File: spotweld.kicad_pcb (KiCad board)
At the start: 2 copper layers, 85.9 x 58.9 mm, 48 parts, among them J1 Conn_02x03_Odd_Even, J2 Conn_01x02, J5 Conn_01x02, Q1 IRF3205, Q2 IRF3205, Q3 IRF3205, Q4 IRF3205, Q5 IRF3205, Q6 IRF3205, Q7 IRF3205, Q8 IRF3205, SW1 SW_Push, U1 ATtiny24-20SSU, U2 TC4429VOA, U3 L78L05_SOT89

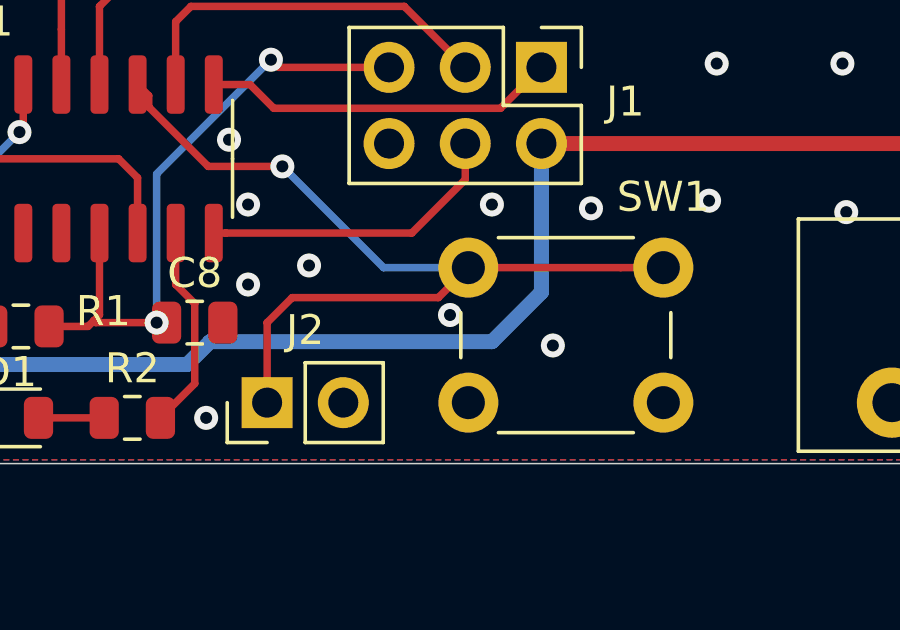
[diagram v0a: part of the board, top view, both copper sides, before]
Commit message: Correct via clearence
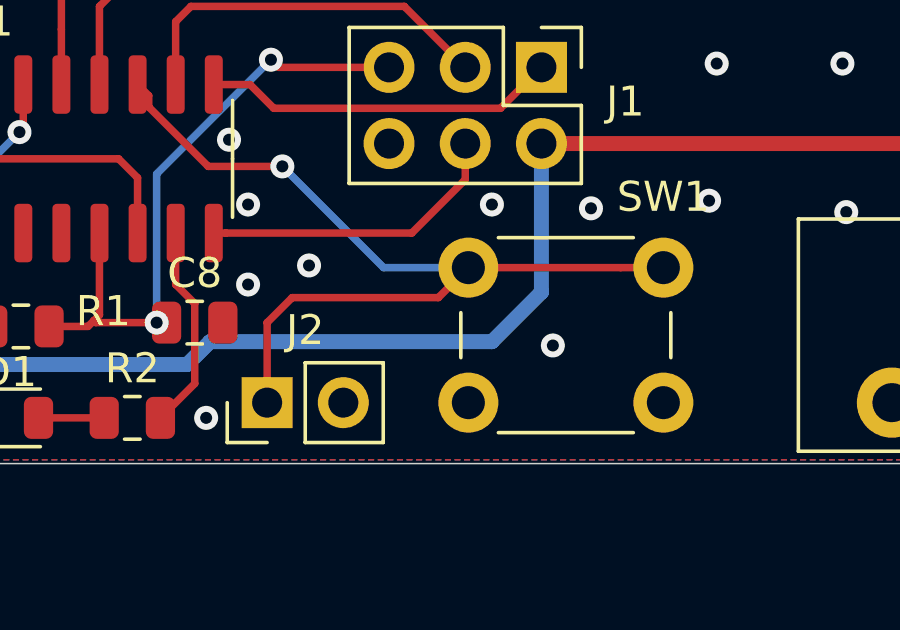
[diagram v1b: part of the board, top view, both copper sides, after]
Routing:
- net GND: vias 42 -> 41
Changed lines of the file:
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@@
     (thickness 1.6)
     (drawings 6)
-    (tracks 291)
+    (tracks 290)
     (zones 0)
     (modules 48)
@@
       (outputformat 1)
       (mirror false)
-      (drillshape 1)
+      (drillshape 0)
       (scaleselection 1)
-      (outputdirectory ""))
+      (outputdirectory "/mnt/store/Bango/ALLPROJECTS/spot-welder/spotweld/gerbers/"))
   )
   (net 0 "")
@@
     (add_net Vdrive)
   )
+  (module Button_Switch_THT:SW_PUSH_6mm_H5mm (layer F.Cu)
+    (at 151.892 119.634 180)
+    (descr "tactile push button, 6x6mm e.g. PHAP33xx series, height=5mm")
+    (tags "tact sw push 6mm")
+    (fp_text reference SW1 (at 0 6.858) (layer F.SilkS)
+      (effects (font (size 1 1) (thickness 0.15)))
+    )
+    (fp_text value SW_Push (at 3.75 6.7) (layer F.Fab)
+      (effects (font (size 1 1) (thickness 0.15)))
+    )
+    (fp_circle (center 3.25 2.25) (end 1.25 2.5) (layer F.Fab) (width 0.1))
+    (fp_line (start 6.75 3) (end 6.75 1.5) (layer F.SilkS) (width 0.12))
+    (fp_line (start 5.5 -1) (end 1 -1) (layer F.SilkS) (width 0.12))
+    (fp_line (start -0.25 1.5) (end -0.25 3) (layer F.SilkS) (width 0.12))
+    (fp_line (start 1 5.5) (end 5.5 5.5) (layer F.SilkS) (width 0.12))
+    (fp_line (start 8 -1.25) (end 8 5.75) (layer F.CrtYd) (width 0.05))
+    (fp_line (start 7.75 6) (end -1.25 6) (layer F.CrtYd) (width 0.05))
+    (fp_line (start -1.5 5.75) (end -1.5 -1.25) (layer F.CrtYd) (width 0.05))
+    (fp_line (start -1.25 -1.5) (end 7.75 -1.5) (layer F.CrtYd) (width 0.05))
+    (fp_line (start -1.5 6) (end -1.25 6) (layer F.CrtYd) (width 0.05))
+    (fp_line (start -1.5 5.75) (end -1.5 6) (layer F.CrtYd) (width 0.05))
+    (fp_line (start -1.5 -1.5) (end -1.25 -1.5) (layer F.CrtYd) (width 0.05))
+    (fp_line (start -1.5 -1.25) (end -1.5 -1.5) (layer F.CrtYd) (width 0.05))
+    (fp_line (start 8 -1.5) (end 8 -1.25) (layer F.CrtYd) (width 0.05))
+    (fp_line (start 7.75 -1.5) (end 8 -1.5) (layer F.CrtYd) (width 0.05))
+    (fp_line (start 8 6) (end 8 5.75) (layer F.CrtYd) (width 0.05))
+    (fp_line (start 7.75 6) (end 8 6) (layer F.CrtYd) (width 0.05))
+    (fp_line (start 0.25 -0.75) (end 3.25 -0.75) (layer F.Fab) (width 0.1))
+    (fp_line (start 0.25 5.25) (end 0.25 -0.75) (layer F.Fab) (width 0.1))
+    (fp_line (start 6.25 5.25) (end 0.25 5.25) (layer F.Fab) (width 0.1))
+    (fp_line (start 6.25 -0.75) (end 6.25 5.25) (layer F.Fab) (width 0.1))
+    (fp_line (start 3.25 -0.75) (end 6.25 -0.75) (layer F.Fab) (width 0.1))
+    (fp_text user %R (at 3.048 2.25) (layer F.Fab)
+      (effects (font (size 1 1) (thickness 0.15)))
+    )
+    (pad 1 thru_hole circle (at 6.5 0 270) (size 2 2) (drill 1.1) (layers *.Cu *.Mask)
+      (net 1 GND))
+    (pad 2 thru_hole circle (at 6.5 4.5 270) (size 2 2) (drill 1.1) (layers *.Cu *.Mask)
+      (net 17 "Net-(J2-Pad1)"))
+    (pad 1 thru_hole circle (at 0 0 270) (size 2 2) (drill 1.1) (layers *.Cu *.Mask)
+      (net 1 GND))
+    (pad 2 thru_hole circle (at 0 4.5 270) (size 2 2) (drill 1.1) (layers *.Cu *.Mask)
+      (net 17 "Net-(J2-Pad1)"))
+    (model ${KISYS3DMOD}/Button_Switch_THT.3dshapes/SW_PUSH_6mm_H5mm.wrl
+      (at (xyz 0 0 0))
+      (scale (xyz 1 1 1))
+      (rotate (xyz 0 0 0))
+    )
+  )
   (module Package_TO_SOT_THT:TO-220-3_Horizontal_TabDown (layer F.Cu)
     (at 181.864 82.804)
@@
       (net 2 VCC))
     (model ${KISYS3DMOD}/Package_SO.3dshapes/SOIC-14_3.9x8.7mm_P1.27mm.wrl
-      (at (xyz 0 0 0))
-      (scale (xyz 1 1 1))
-      (rotate (xyz 0 0 0))
-    )
-  )
-  (module Button_Switch_THT:SW_PUSH_6mm_H5mm (layer F.Cu)
-    (at 151.892 119.634 180)
-    (descr "tactile push button, 6x6mm e.g. PHAP33xx series, height=5mm")
-    (tags "tact sw push 6mm")
-    (fp_text reference SW1 (at 0 6.858) (layer F.SilkS)
-      (effects (font (size 1 1) (thickness 0.15)))
-    )
-    (fp_text value SW_Push (at 3.75 6.7) (layer F.Fab)
-      (effects (font (size 1 1) (thickness 0.15)))
-    )
-    (fp_circle (center 3.25 2.25) (end 1.25 2.5) (layer F.Fab) (width 0.1))
-    (fp_line (start 6.75 3) (end 6.75 1.5) (layer F.SilkS) (width 0.12))
-    (fp_line (start 5.5 -1) (end 1 -1) (layer F.SilkS) (width 0.12))
-    (fp_line (start -0.25 1.5) (end -0.25 3) (layer F.SilkS) (width 0.12))
-    (fp_line (start 1 5.5) (end 5.5 5.5) (layer F.SilkS) (width 0.12))
-    (fp_line (start 8 -1.25) (end 8 5.75) (layer F.CrtYd) (width 0.05))
-    (fp_line (start 7.75 6) (end -1.25 6) (layer F.CrtYd) (width 0.05))
-    (fp_line (start -1.5 5.75) (end -1.5 -1.25) (layer F.CrtYd) (width 0.05))
-    (fp_line (start -1.25 -1.5) (end 7.75 -1.5) (layer F.CrtYd) (width 0.05))
-    (fp_line (start -1.5 6) (end -1.25 6) (layer F.CrtYd) (width 0.05))
-    (fp_line (start -1.5 5.75) (end -1.5 6) (layer F.CrtYd) (width 0.05))
-    (fp_line (start -1.5 -1.5) (end -1.25 -1.5) (layer F.CrtYd) (width 0.05))
-    (fp_line (start -1.5 -1.25) (end -1.5 -1.5) (layer F.CrtYd) (width 0.05))
-    (fp_line (start 8 -1.5) (end 8 -1.25) (layer F.CrtYd) (width 0.05))
-    (fp_line (start 7.75 -1.5) (end 8 -1.5) (layer F.CrtYd) (width 0.05))
-    (fp_line (start 8 6) (end 8 5.75) (layer F.CrtYd) (width 0.05))
-    (fp_line (start 7.75 6) (end 8 6) (layer F.CrtYd) (width 0.05))
-    (fp_line (start 0.25 -0.75) (end 3.25 -0.75) (layer F.Fab) (width 0.1))
-    (fp_line (start 0.25 5.25) (end 0.25 -0.75) (layer F.Fab) (width 0.1))
-    (fp_line (start 6.25 5.25) (end 0.25 5.25) (layer F.Fab) (width 0.1))
-    (fp_line (start 6.25 -0.75) (end 6.25 5.25) (layer F.Fab) (width 0.1))
-    (fp_line (start 3.25 -0.75) (end 6.25 -0.75) (layer F.Fab) (width 0.1))
-    (fp_text user %R (at 3.048 2.25) (layer F.Fab)
-      (effects (font (size 1 1) (thickness 0.15)))
-    )
-    (pad 1 thru_hole circle (at 6.5 0 270) (size 2 2) (drill 1.1) (layers *.Cu *.Mask)
-      (net 1 GND))
-    (pad 2 thru_hole circle (at 6.5 4.5 270) (size 2 2) (drill 1.1) (layers *.Cu *.Mask)
-      (net 17 "Net-(J2-Pad1)"))
-    (pad 1 thru_hole circle (at 0 0 270) (size 2 2) (drill 1.1) (layers *.Cu *.Mask)
-      (net 1 GND))
-    (pad 2 thru_hole circle (at 0 4.5 270) (size 2 2) (drill 1.1) (layers *.Cu *.Mask)
-      (net 17 "Net-(J2-Pad1)"))
-    (model ${KISYS3DMOD}/Button_Switch_THT.3dshapes/SW_PUSH_6mm_H5mm.wrl
       (at (xyz 0 0 0))
       (scale (xyz 1 1 1))
@@
   (via (at 149.479 113.157) (size 0.8) (drill 0.4) (layers F.Cu B.Cu) (net 1))
   (via (at 148.209 117.729) (size 0.8) (drill 0.4) (layers F.Cu B.Cu) (net 1))
-  (via (at 144.78 116.713) (size 0.8) (drill 0.4) (layers F.Cu B.Cu) (net 1))
   (via (at 162.306 113.411) (size 0.8) (drill 0.4) (layers F.Cu B.Cu) (net 1))
   (via (at 162.306 116.332) (size 0.8) (drill 0.4) (layers F.Cu B.Cu) (net 1))
